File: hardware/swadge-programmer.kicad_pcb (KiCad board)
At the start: 2 copper layers, 73.7 x 73.7 mm, 24 parts, among them J1 USB_B_Micro, J2 Conn_02x21_Top_Bottom, J3 Conn_02x21_Top_Bottom, SW1 SW_DPDT_x2, SW2 SW_DPDT_x2, SW3 SW_DPDT_x2, SW4 SW_DPDT_x2, SW5 SW_DPDT_x2, U1 BUS_PCIexpress, U2 CP2102N-A01-GQFN24

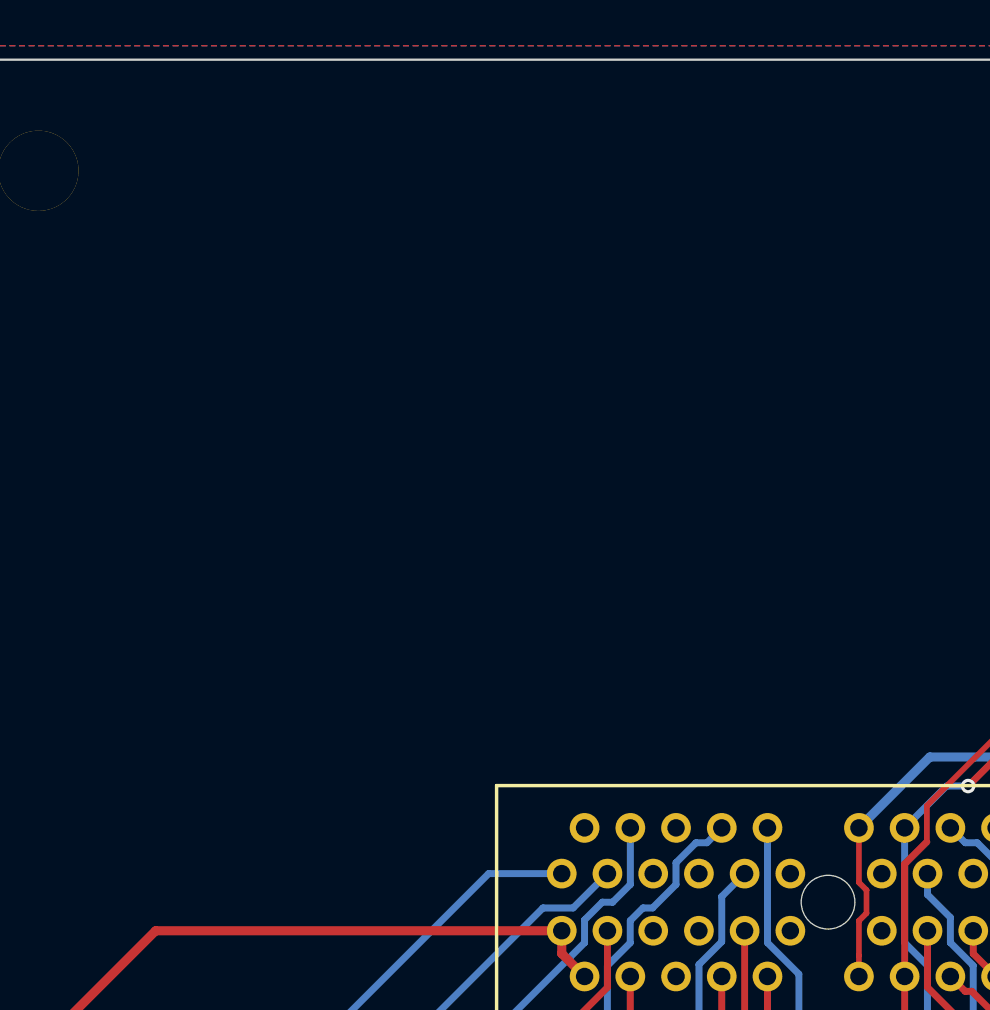
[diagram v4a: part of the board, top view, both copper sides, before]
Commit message: Updated digikey part numbers Added graphics to swadge programmer PCB
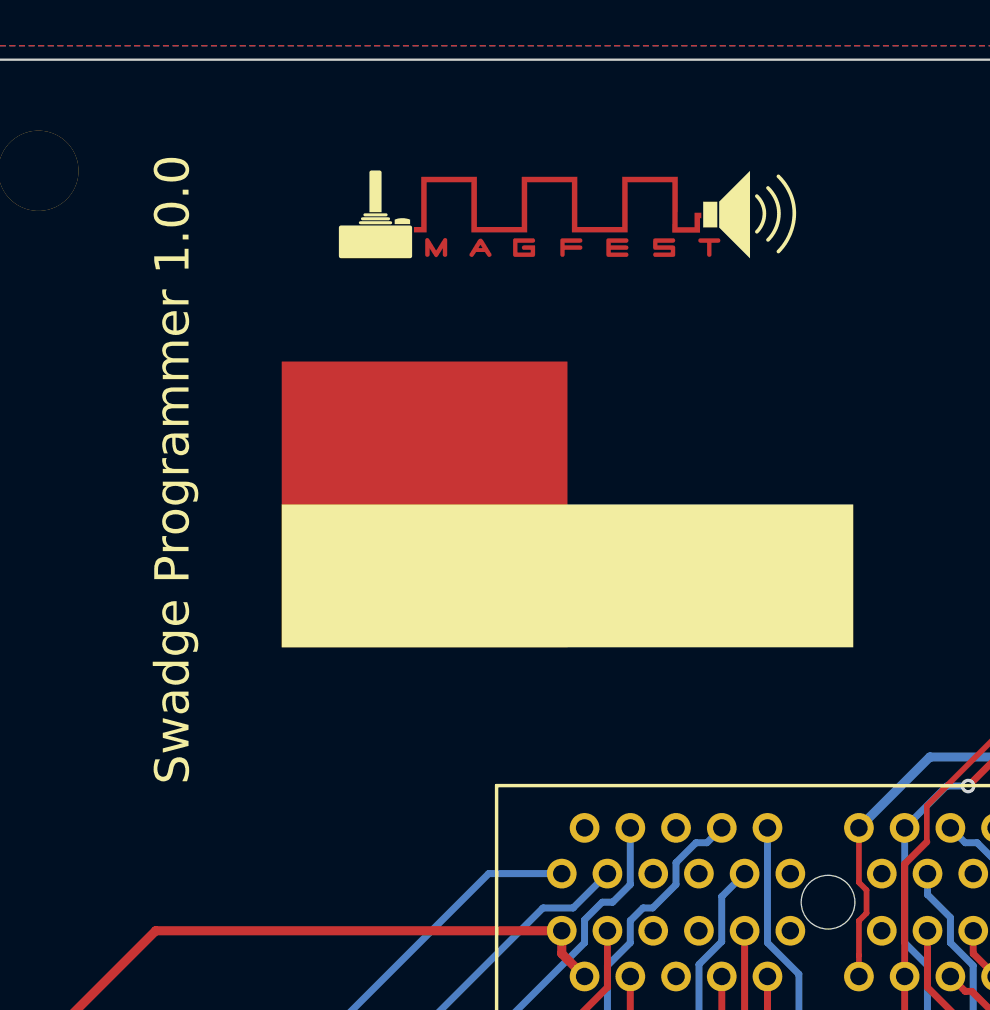
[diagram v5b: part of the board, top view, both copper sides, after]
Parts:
- added svg2mod: G***, Swadge_Parts:MAGFEST_logo_centered_final, F.Cu at (136.1, 56.9)
- added svg2mod: G***, Swadge_Parts:pcb_color_swatches, F.Cu at (136.1, 69.6)
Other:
- board text added: "Swadge Programmer 1.0.0"

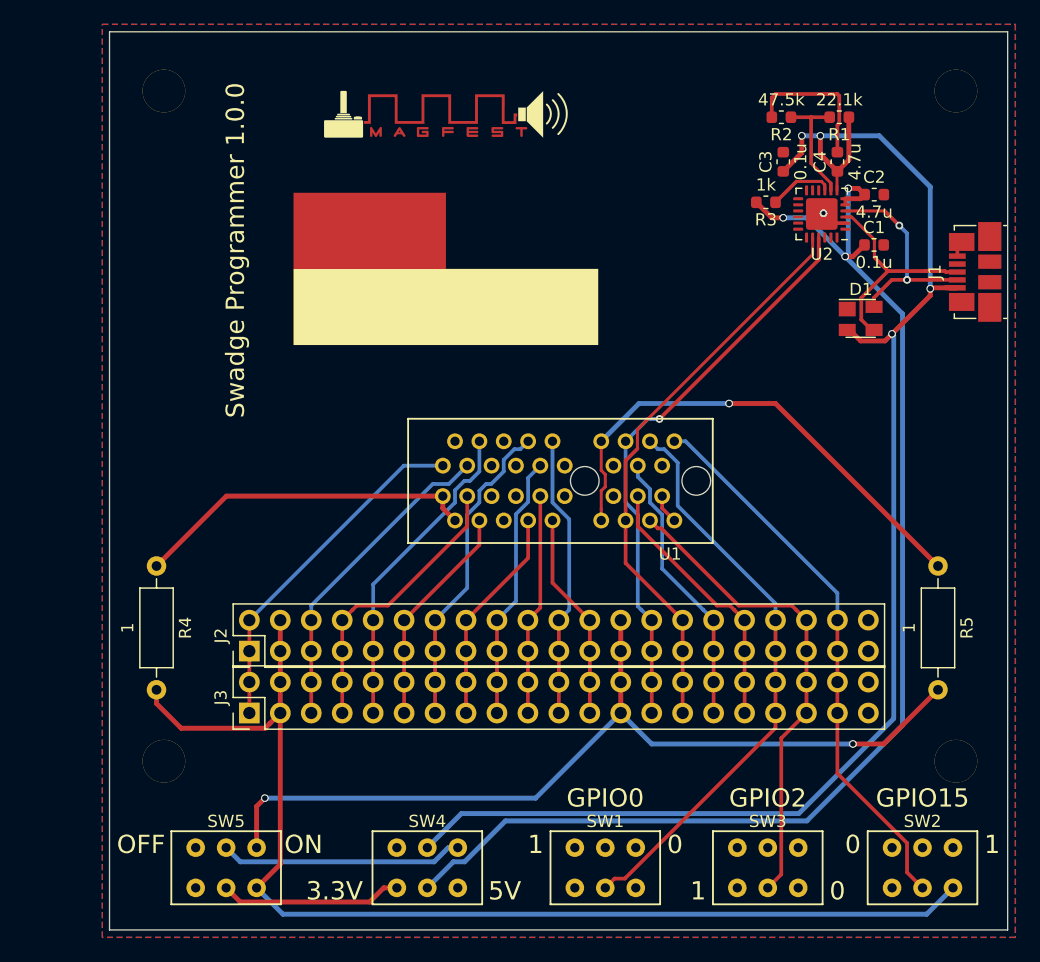
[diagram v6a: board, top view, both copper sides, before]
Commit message: #1 #2 #3 #5 #6 #7 #16 Routed PCB
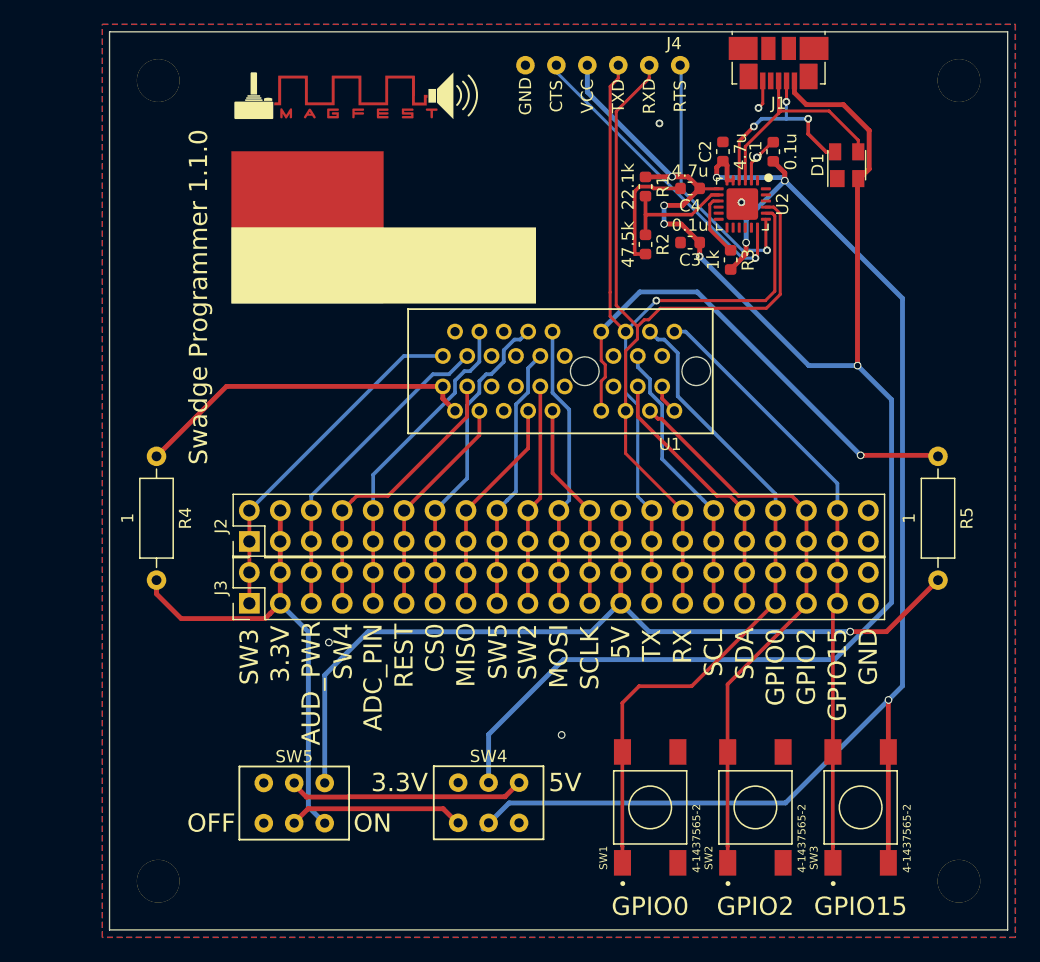
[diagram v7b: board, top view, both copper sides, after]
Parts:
- added J4: ftdi-header, Swadge_Parts:ftdi-header, F.Cu at (149.0, 52.9)
- SW1, SW2, SW3: value SW_DPDT_x2 -> 4-1437565-2; footprint Swadge_Parts:JS202011CQN -> Swadge_Parts:SW_4-1437565-2
- moved J1 23.5 mm to (163.4, 52.7), turned to 180 degrees
- moved R1 16.9 mm to (152.5, 62.8), turned to 270 degrees
- moved R2 15.3 mm to (152.5, 67.6), turned to 270 degrees
- moved SW2 14.6 mm to (161.5, 113.8), turned to 90 degrees
- moved C2 12.9 mm to (158.9, 60.0), turned to 90 degrees
- moved D1 12.6 mm to (169.0, 61.1), turned to 90 degrees
- moved C4 12.3 mm to (156.2, 63.0), turned to 180 degrees
- moved C1 11.3 mm to (163.0, 60.0), turned to 90 degrees
- moved C3 10.1 mm to (156.2, 67.4), turned to 180 degrees
- moved H2 9.86 mm to (112.5, 119.8)
- moved H4 9.85 mm to (178.2, 119.8)
- moved SW3 9.09 mm to (170.2, 113.8), turned to 90 degrees
- moved J2 9.00 mm to (120.0, 92.0)
- moved J3 9.00 mm to (120.0, 97.0)
- moved R4 9.00 mm to (112.4, 85.0)
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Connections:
- SW1 pad 1: (no net) -> GPIO0
- SW1 pad 4: (no net) -> GND
- SW2 pad 1: (no net) -> GPIO2
- SW2 pad 2: GPIO15 -> GPIO2
- SW2 pad 3: 3.3V -> GND
- SW2 pad 4: (no net) -> GND
- SW3 pad 1: (no net) -> GPIO15
- SW3 pad 2: GPIO2 -> GPIO15
- SW3 pad 3: GND -> +3V3
- SW3 pad 4: (no net) -> +3V3
- U2 pad 18: (no net) -> CTS
- U2 pad 19: (no net) -> RTS
- U2 pad 20: RX -> TX
- U2 pad 21: TX -> RX
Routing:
- net 3.3V: track 94.4 -> 39.9 mm
- net CTS: track 0.00 -> 25.8 mm, vias 0 -> 1
- net RX: track 47.3 -> 69.3 mm
- net RTS: track 0.00 -> 21.9 mm, vias 0 -> 1
- net TX: track 47.0 -> 66.5 mm
- net +5V: track 120.9 -> 135.1 mm, vias 4 -> 5
- net +3V3: track 105.5 -> 118.7 mm, vias 3 -> 4
- net GPIO2: track 39.5 -> 48.0 mm
- net GPIO0: track 47.5 -> 55.8 mm
- net GPIO15: track 45.6 -> 49.7 mm
- net GND: track 17.9 -> 19.8 mm, vias 1 -> 6
- net 5V: track 73.0 -> 71.8 mm, vias 2 -> 1
- net Net-(D1-Pad4): track 17.8 -> 16.8 mm, vias 2 -> 3
- net Net-(D1-Pad3): track 18.6 -> 18.0 mm
- net Net-(SW4-Pad1): track 15.0 -> 14.4 mm
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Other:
- board text added: "ADC_PIN"
- board text added: "AUD_PWR"
- board text added: "CS0"
- board text added: "GND"
- board text added: "MISO"
- board text added: "MOSI"
- board text added: "REST"
- board text added: "RX"
- board text added: "SCL"
- board text added: "SCLK"
- board text added: "SDA"
- board text added: "SW2"
- board text added: "SW3"
- board text added: "SW4"
- board text added: "SW5"
- board text added: "Swadge Programmer 1.1.0"
- board text added: "TX"
- board text removed: "0"
- board text removed: "1"
- board text removed: "Swadge Programmer 1.0.0"

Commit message: Swapped RX/TX on FTDI header, added voltage jumper selector
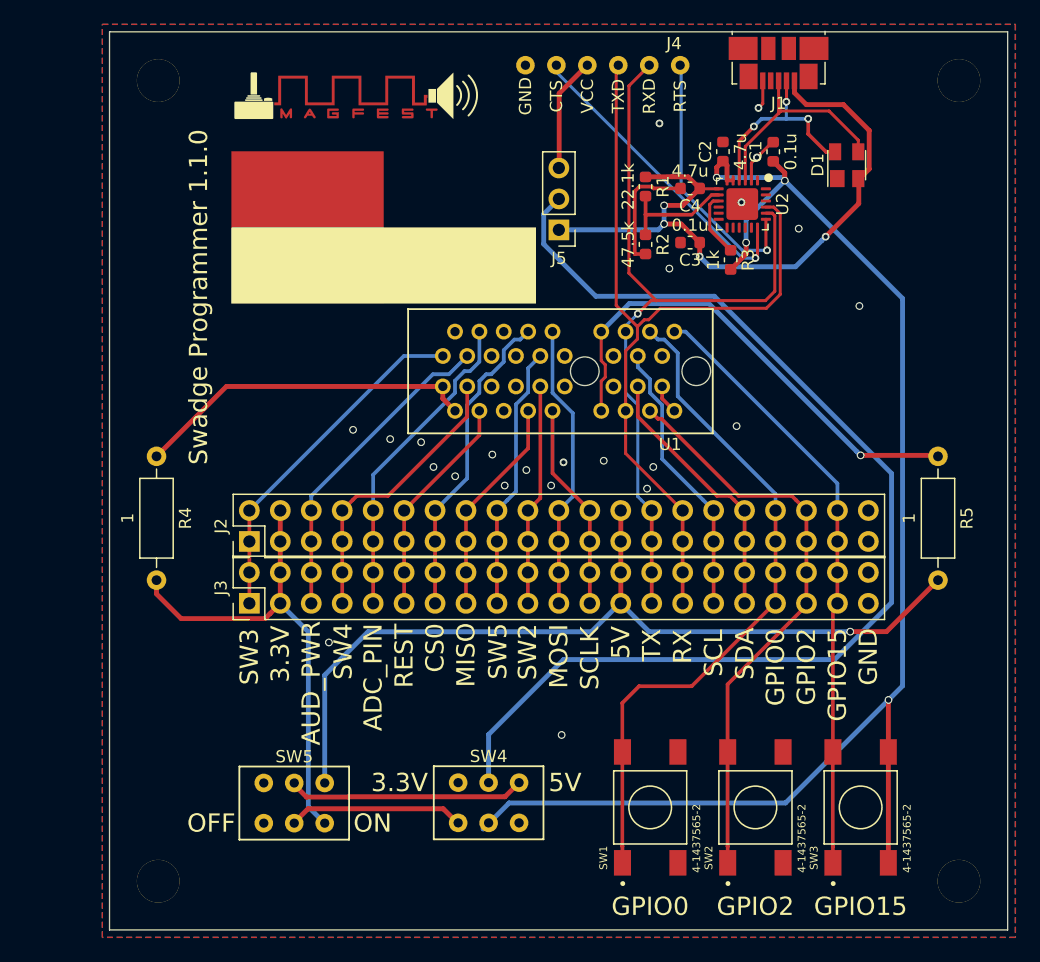
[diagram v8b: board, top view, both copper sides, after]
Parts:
- added J5: Conn_01x03_Male, Swadge_Parts:PinHeader_1x03_P2.54mm_Vertical, F.Cu at (145.4, 66.4)
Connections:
- C3 pad 1: +5V -> Net-(C3-Pad1)
- C4 pad 1: +5V -> Net-(C3-Pad1)
- D1 pad 2: +5V -> Net-(C3-Pad1)
- J1 pad 1: +5V -> Net-(C3-Pad1)
- J4 pad 2: CTS -> RTS
- J4 pad 3: +5V -> Net-(J4-Pad3)
- J4 pad 4: TX -> RX
- J4 pad 5: RX -> TX
- J4 pad 6: RTS -> CTS
- R1 pad 1: +5V -> Net-(C3-Pad1)
- U2 pad 18: CTS -> RTS
- U2 pad 19: RTS -> CTS
- U2 pad 7: +5V -> Net-(C3-Pad1)
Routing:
- net Net-(C3-Pad1): track 0.00 -> 55.3 mm, vias 0 -> 4
- net +5V: track 135.1 -> 92.7 mm, vias 5 -> 0
- net Net-(J4-Pad3): track 0.00 -> 9.39 mm
- net RTS: track 21.9 -> 25.8 mm
- net CTS: track 25.8 -> 21.9 mm
- net TX: track 66.5 -> 65.1 mm
- net RX: track 69.3 -> 68.1 mm
- net Net-(R5-Pad1): track 41.3 -> 40.5 mm
- net GND: vias 6 -> 23
